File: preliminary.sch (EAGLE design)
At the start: 35 parts, among them IC1 STM32F407VGT6, Q1 600mA/40V, U1 STMPS2141STR, Y1 8MHz

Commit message: Review
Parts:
- added C17: 0.1uF, SparkFun-Capacitors:0.1UF-0603-25V-(+80/-20%)
- added C18: 200pF, SparkFun-Capacitors:0.1UF-0603-25V-(+80/-20%)
- added C19, C20: 100nF, SparkFun-Capacitors:3.0NF-0603-50V-5%
- added C21, C22: 2.2uF, SparkFun-Capacitors:4.7UF0603
- added C23, C24: 1uF, SparkFun-Capacitors:22PF-0603-50V-5%
- added D3, D4, D5: BLUE, SparkFun-LED:LED-BLUE0603
- added J2: (no value), SparkFun-Connectors:CONN_03X2FEMALE_SMD
- added J3: POWER_JACK, SparkFun-Connectors:POWER_JACK
- added MK1: SPH0645LM4H-B, SPH0645LM4H-B:SPH0645LM4H-B
- added R12: 330, SparkFun-Resistors:220KOHM-0603-1/10W-1%
- added R13: 100, SparkFun-Resistors:220KOHM-0603-1/10W-1%
- added R14, R15: 10k, SparkFun-Resistors:2.2KOHM-0603-1/10W-1%
- added R16: 0, SparkFun-Resistors:220KOHM-0603-1/10W-1%
- added R17: 10k, SparkFun-Resistors:220KOHM-0603-1/10W-1%
- added R18, R19, R20, R21: 22, SparkFun-Resistors:220KOHM-0603-1/10W-1%
- added S1, S2: (no value), SparkFun-Switches:MOMENTARY-SWITCH-SPST-2-SMD-4.6X2.8MM
- added U$2: ESP01, esp8266modules:ESP01
- added U$3: EMIF02-USB03F2, EMIF02-USB03F2:EMIF02-USB03F2
- added U2: 3.3V, SparkFun-IC-Power:V_REG_AP2112K-3.3V
- R1: value 4.7k -> 220k; device SparkFun-Resistors:4.7KOHM-0603-1/10W-1% -> SparkFun-Resistors:220KOHM-0603-1/10W-1%
- R2: value 4.7k -> 10k; device SparkFun-Resistors:4.7KOHM-0603-1/10W-1% -> SparkFun-Resistors:2.2KOHM-0603-1/10W-1%
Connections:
- removed net PB6: IC1.PB6, R2.1
- removed net PB9: IC1.PB9, R1.1
- new net 3V: C24.2, U2.OUT
- new net 5V: C23.2, J3.PWR, U2.EN, U2.IN
- new net N$11: D3.A, R2.1
- new net N$12: J2.2, R18.1
- new net N$13: IC1.PD14, R15.2
- new net N$14: IC1.PD13, R14.2
- new net N$15: C20.1, R13.1
- new net N$16: IC1.PD12, R2.2
- new net N$17: D4.A, R14.1
- new net N$18: D5.A, R15.1
- new net N$19: C21.1, IC1.VCAP_2
- new net N$20: C22.1, IC1.VCAP_1
- new net N$21: J2.5, R19.2
- new net N$22: J2.1, R17.2
- new net N$24: J2.4, R20.1
- new net N$26: J2.6, R21.1
- new net N$4: C20.2, R1.2, R12.2, S2.3, S2.4
- new net NRST: C19.1, IC1.NRST, R19.1, S1.3, S1.4
- new net PA0: IC1.PA0, R12.1
- new net PA13: IC1.PA13, R20.2
- new net PA14: IC1.PA14, R18.2
- new net PB10: IC1.PB10, MK1.BCLK
- new net PB3: IC1.PB3, R21.2
- new net PC10: IC1.PC10, U$2.RXD
- new net PC11: IC1.PC11, U$2.TXD
- new net PC12: IC1.PC12, U$2.GPIO2
- new net PC3: IC1.PC3, MK1.DATA_OUT
- new net PC9: IC1.PC9, U$2.GPIO0
- net GND: now also C17.2, C18.2, C19.2, C21.2, C22.2, C23.1, C24.1, D3.C, D4.C, D5.C, IC1.BOOT0, IC1.VSS, IC1.VSSA, J2.3, J3.GND, J3.GNDBREAK, MK1.GND, Q1.E, R1.1, S1.1, S1.2, U$2.GND, U$3.GND, U2.GND
- net N$6: now also U$3.DM-IN
- net N$7: now also U$3.DP-IN
- net PA10: now also U$3.ID
- net PA11: now also R8.1, U$3.DM-OUT; no longer R9.1
- net PA12: now also R9.1, U$3.DP-OUT; no longer R8.1
- net PA9: now also U$3.VBUS
- net VBAT: now also IC1.VBAT, R16.2; no longer C10.1, C11.1, C12.1, C13.1, C6.1, C7.1, C8.1, C9.1, U$1.1.IN
- net VDD: now also C10.1, C11.1, C12.1, C13.1, C17.1, C18.1, C6.1, C7.1, C8.1, C9.1, IC1.VDD, MK1.SELECT, MK1.VDD, MK1.WS, R13.2, R16.1, R17.1, S2.1, S2.2, U$1.1.IN, U$2.CH_PD, U$2.RST, U$2.VCC; no longer R1.2, R2.2
- net VDDA: now also IC1.VDDA
- net VREF+: now also IC1.VREF+
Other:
- moved on the sheet: C16, D1, D2, J1, Q1, R1, R10, R11, R2, R5, R6, R7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

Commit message: Schematic changed
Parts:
- removed D2: SFH482, led:SFH482
- removed D5: BLUE, SparkFun-LED:LED-BLUE0603
- removed S2: (no value), SparkFun-Switches:MOMENTARY-SWITCH-SPST-2-SMD-4.6X2.8MM
- removed U2: 3.3V, SparkFun-IC-Power:V_REG_AP2112K-3.3V
- added C25, C26, C27: 47uF, SparkFun-Capacitors:10UF-1206-6.3V-20%
- added C28: 10uF, SparkFun-Capacitors:10UF-0603-6.3V-20%
- added D6: SFH482, led:SFH482
- added D7: BLUE, SparkFun-LED:LED-BLUE0603
- added J4: (no value), SparkFun-Connectors:CONN_02
- added R22: 0, SparkFun-Resistors:0.05OHM-0603-1/5W-1%
- added U$4: TPSM5, preliminary:TPSM5
- added U$5: TPSM3.3, preliminary:TPSM3.3
- C23: value 1uF -> 10uF; device SparkFun-Capacitors:22PF-0603-50V-5% -> SparkFun-Capacitors:10UF-0603-6.3V-20%
- C24: value 1uF -> 47uF; device SparkFun-Capacitors:22PF-0603-50V-5% -> SparkFun-Capacitors:10UF-1206-6.3V-20%
- D1: value SFH482 -> BLUE; device led:SFH482 -> SparkFun-LED:LED-BLUE0603
- D3, D4: value BLUE -> SFH482; device SparkFun-LED:LED-BLUE0603 -> led:SFH482
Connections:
- removed net 3V: C24.2, U2.OUT
- removed net 5V: C23.2, J3.PWR, U2.EN, U2.IN
- removed net VDD: C10.1, C11.1, C12.1, C13.1, C17.1, C18.1, C6.1, C7.1, C8.1, C9.1, IC1.VDD, MK1.SELECT, MK1.VDD, MK1.WS, R11.2, R13.2, R16.1, R17.1, R5.2, R6.1, R7.1, S2.1, S2.2, U$1.1.IN, U$2.CH_PD, U$2.RST, U$2.VCC, U1.IN
- new net +3V3: C10.1, C11.1, C12.1, C13.1, C17.1, C18.1, C26.1, C27.1, C6.1, C7.1, C8.1, C9.1, IC1.VDD, J4.1, MK1.SELECT, MK1.VDD, MK1.WS, R11.2, R13.2, R16.1, R17.1, R5.2, R6.1, R7.1, U$1.1.IN, U$2.CH_PD, U$2.RST, U$2.VCC, U$5.V_OUT
- new net +5V: C24.1, C25.1, C28.1, U$4.V_OUT, U1.IN
- new net N$23: C23.1, J3.PWR, U$4.V_IN
- new net N$25: IC1.BOOT0, R22.2
- net GND: now also C23.2, C24.2, C25.2, C26.2, C27.2, C28.2, D6.C, R22.1, U$4.GND, U$5.GND; no longer C23.1, C24.1, D3.C, D4.C, D5.C, IC1.BOOT0, U2.GND
- net N$10: now also D1.A; no longer D2.A
- net N$11: now also D6.A; no longer D3.A
- net N$17: no longer D4.A
- net N$18: no longer D5.A
- net N$4: now also J4.2; no longer S2.3, S2.4
- net N$5: now also D7.A; no longer D1.A
- net N$9: now also D1.C; no longer D2.C
- net PD5: now also D7.C; no longer D1.C
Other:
- moved on the sheet: C23, C24

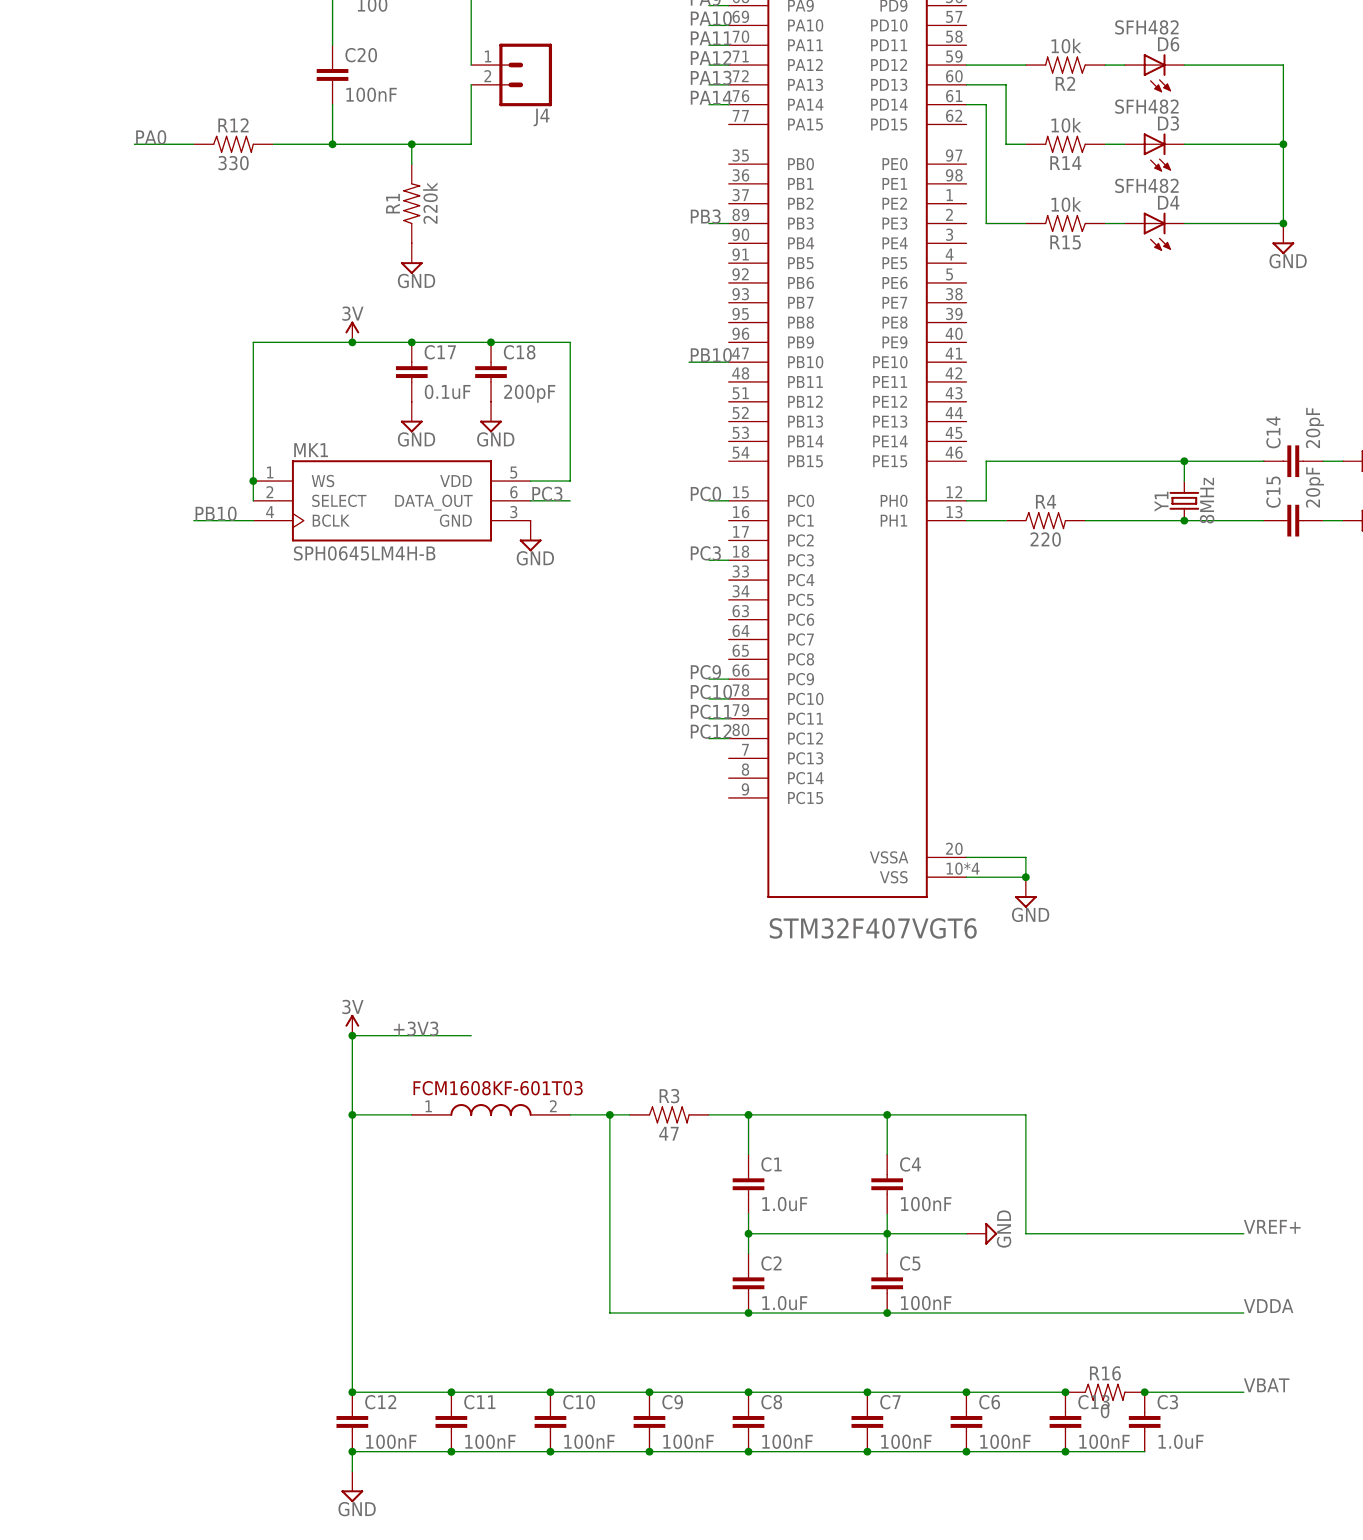
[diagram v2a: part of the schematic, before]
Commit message: Placing components on the PCB
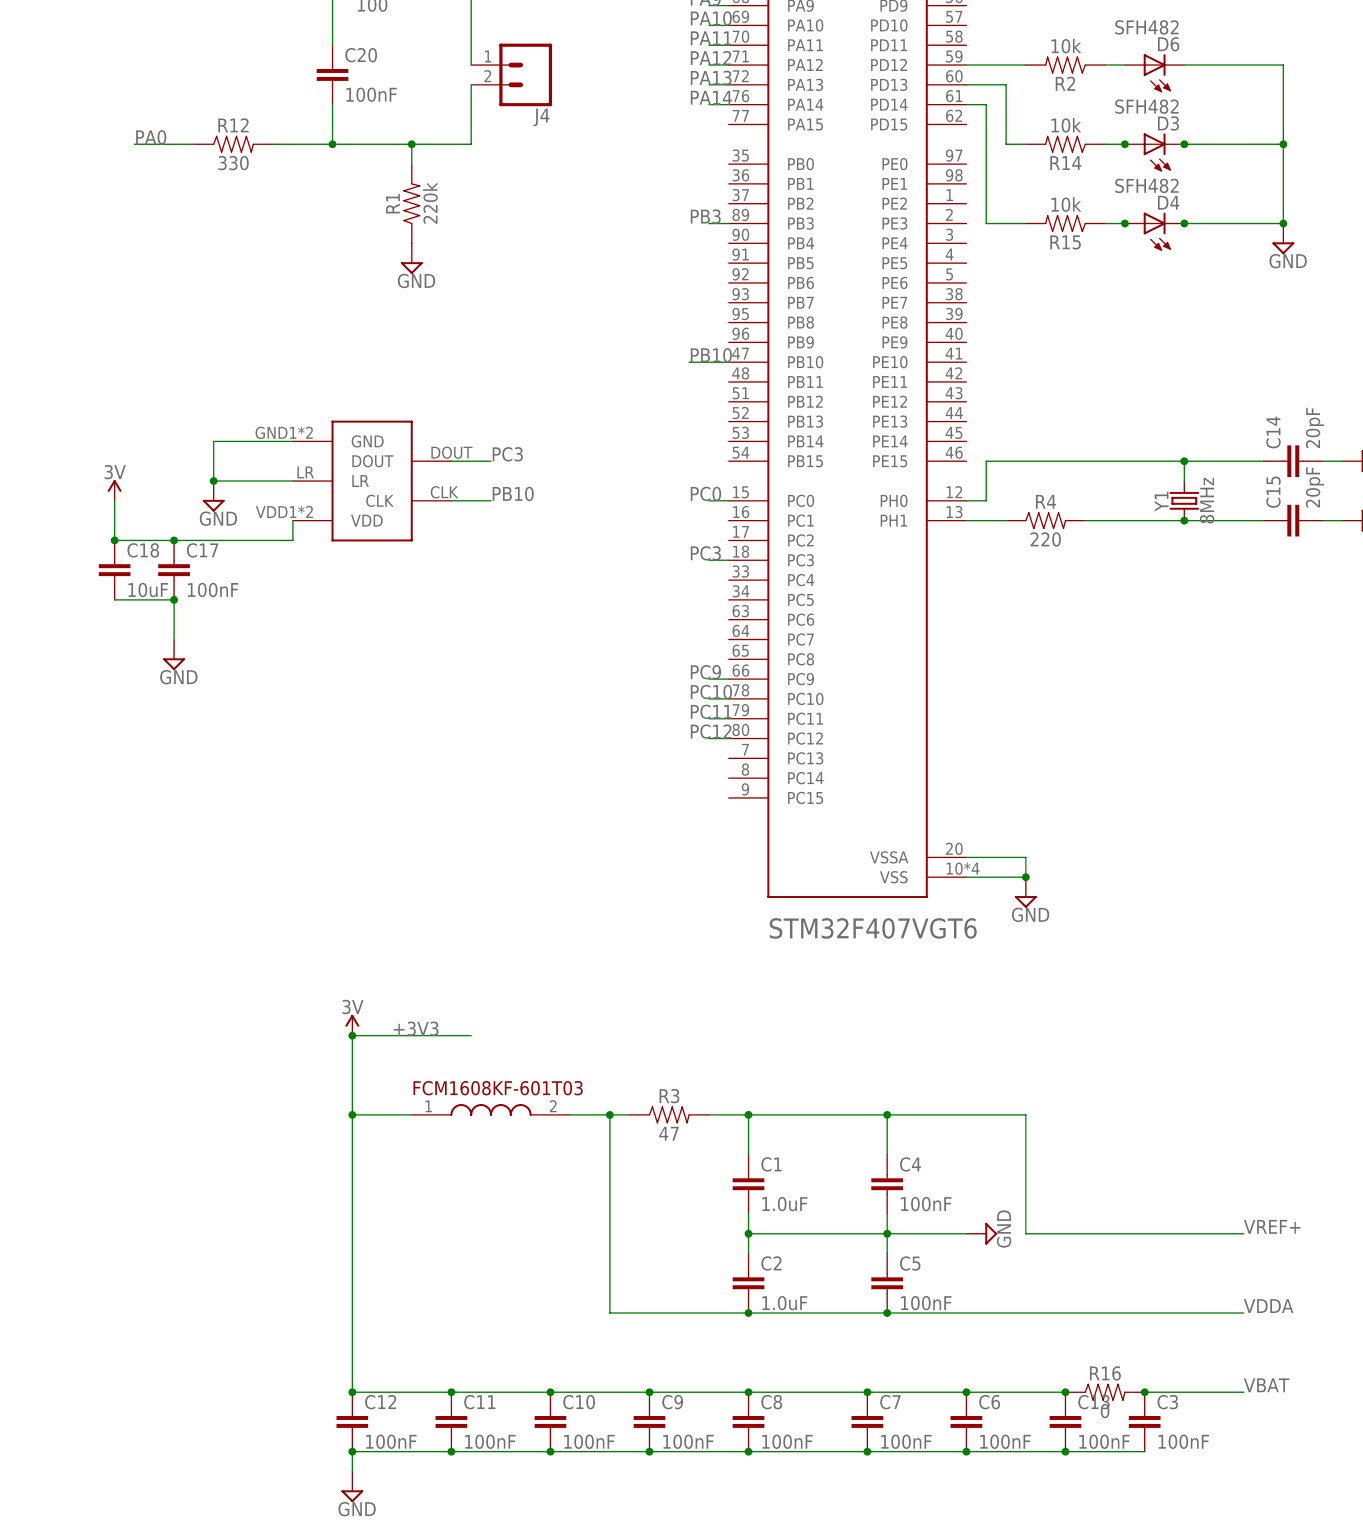
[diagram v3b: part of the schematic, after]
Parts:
- removed MK1: SPH0645LM4H-B, SPH0645LM4H-B:SPH0645LM4H-B
- added U$6: MP45DT02-M, preliminary:MP45DT02-M
- C10, C11, C12, C13, C6, C7, C8, C9: device SparkFun-Capacitors:470NF-0402-16V-10% -> SparkFun-Capacitors:10NF-0603-50V-10%
- C17: value 0.1uF -> 100nF; device SparkFun-Capacitors:0.1UF-0603-25V-(+80/-20%) -> SparkFun-Capacitors:10UF-0603-6.3V-20%
- C18: value 200pF -> 10uF; device SparkFun-Capacitors:0.1UF-0603-25V-(+80/-20%) -> SparkFun-Capacitors:10UF-0603-6.3V-20%
- C3: value 1.0uF -> 100nF; device SparkFun-Capacitors:1.0UF-0805-25V-(+80/-20%) -> SparkFun-Capacitors:10NF-0603-50V-10%
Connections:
- new net VDD: C17.1, C18.1, U$6.VDD
- net +3V3: no longer C17.1, C18.1, MK1.SELECT, MK1.VDD, MK1.WS
- net GND: now also D3.C, D4.C, U$6.GND, U$6.LR; no longer MK1.GND
- net N$17: now also D3.A
- net N$18: now also D4.A
- net PB10: now also U$6.CLK; no longer MK1.BCLK
- net PC3: now also U$6.DOUT; no longer MK1.DATA_OUT
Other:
- moved on the sheet: C17, C18

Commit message: 2nd revision finished
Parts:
- removed J1: (no value), SparkFun-Connectors:USB_AB_SMT
- removed U$3: EMIF02-USB03F2, EMIF02-USB03F2:EMIF02-USB03F2
- added H1, H2, H3, H4: STAND-OFF, SparkFun-Hardware:STAND-OFF
- added J5: (no value), SparkFun-Connectors:USB_MICRO-B_SMT
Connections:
- removed net VDD: C17.1, C18.1, U$6.VDD
- net +3V3: now also C17.1, C18.1, U$6.VDD
- net +5V: now also U$5.V_IN
- net GND: now also J5.GND; no longer J1.GND, J1.SHIELD, U$3.GND
- net N$6: now also J5.D-; no longer J1.D-, U$3.DM-IN
- net N$7: now also J5.D+; no longer J1.D+, U$3.DP-IN
- net PA10: now also J5.ID; no longer J1.USBID, U$3.ID
- net PA11: no longer U$3.DM-OUT
- net PA12: no longer U$3.DP-OUT
- net PA9: now also J5.VBUS; no longer J1.VBUS, U$3.VBUS
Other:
- moved on the sheet: R8, R9
